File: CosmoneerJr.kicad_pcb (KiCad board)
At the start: 2 copper layers, 70 x 50 mm, 93 parts, among them J1 Header, J12 Header, J13 Header, J16 Header, J17 Header, J18 Header, J4 Header, J5 Header, J8 Header, J9 Header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

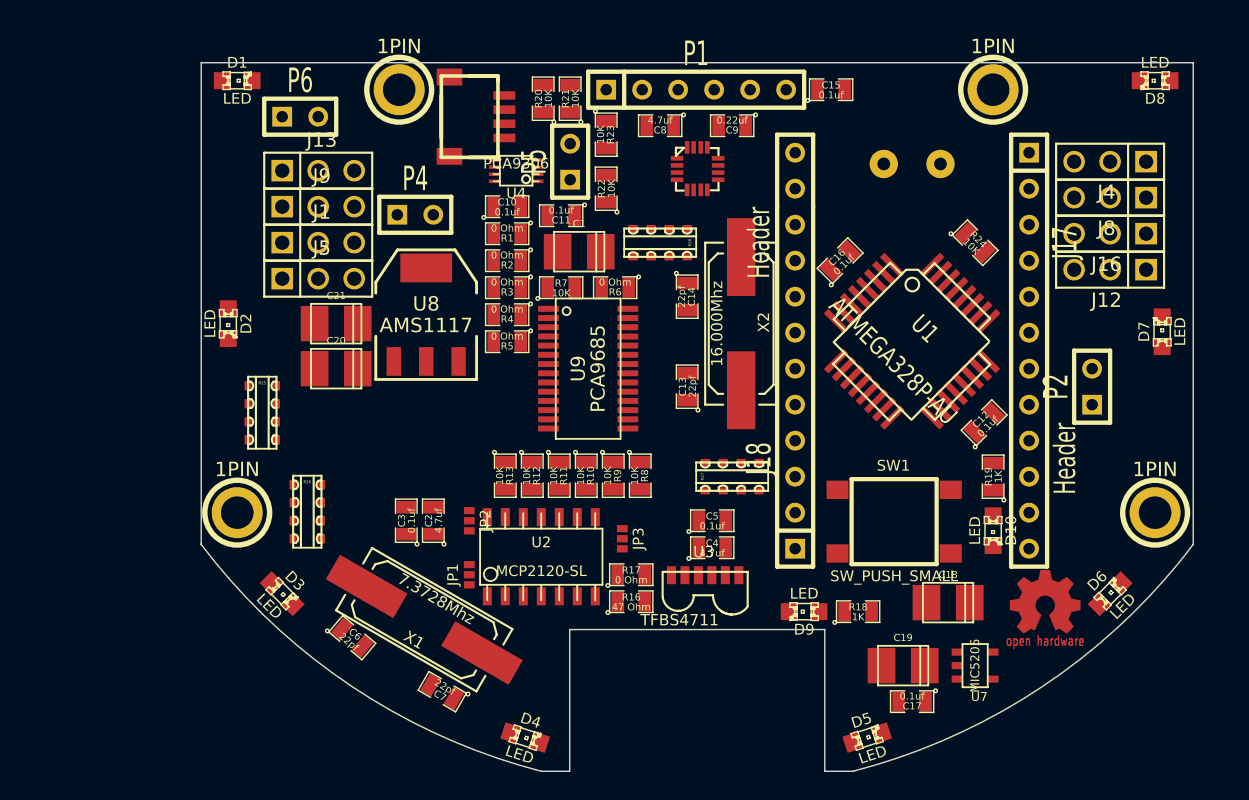
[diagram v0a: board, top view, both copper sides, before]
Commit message: PDF added
Generated a pdf version of the schematic

Schematic fixes made

Net connections on U1 were disconnected during component move.  Nets
reconnected, pdf generated, netlist generated and re-imported into pcb.
PCB file updated and saved.
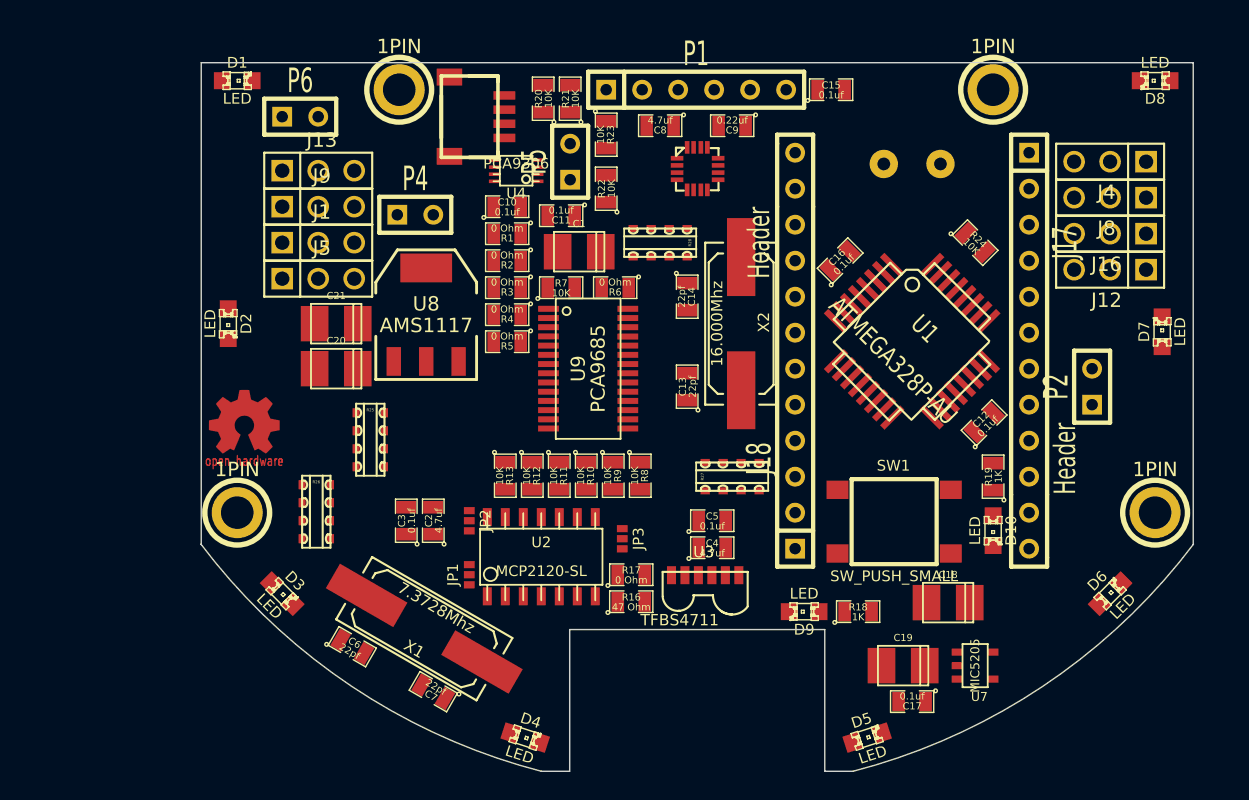
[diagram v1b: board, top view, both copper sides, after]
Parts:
- moved G*** 57.9 mm to (193.0, 140.3)
- moved R25 7.85 mm to (201.9, 141.6)
- moved C6 0.64 mm to (200.7, 156.2), turned to 330 degrees
- moved C7 0.63 mm to (206.4, 159.4)
- moved R26 0.63 mm to (198.1, 146.7)
- moved X1 0.63 mm to (205.7, 154.9)
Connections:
- J17 pad 10: (no net) -> /D7
- J17 pad 6: (no net) -> /D3
- J17 pad 9: (no net) -> /D6
- U1 pad 1: (no net) -> /D3
- U1 pad 10: (no net) -> /D6
- U1 pad 11: (no net) -> /D7
- U1 pad 2: (no net) -> /PIEZO
- U1 pad 30: (no net) -> /RXI
- U1 pad 31: (no net) -> /TXO
- U1 pad 32: (no net) -> /INT
- U1 pad 9: (no net) -> ENABLE

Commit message: Pressfit PCB additions
Added pads, drills and Silkscreen outlines for press fit pcb additions.
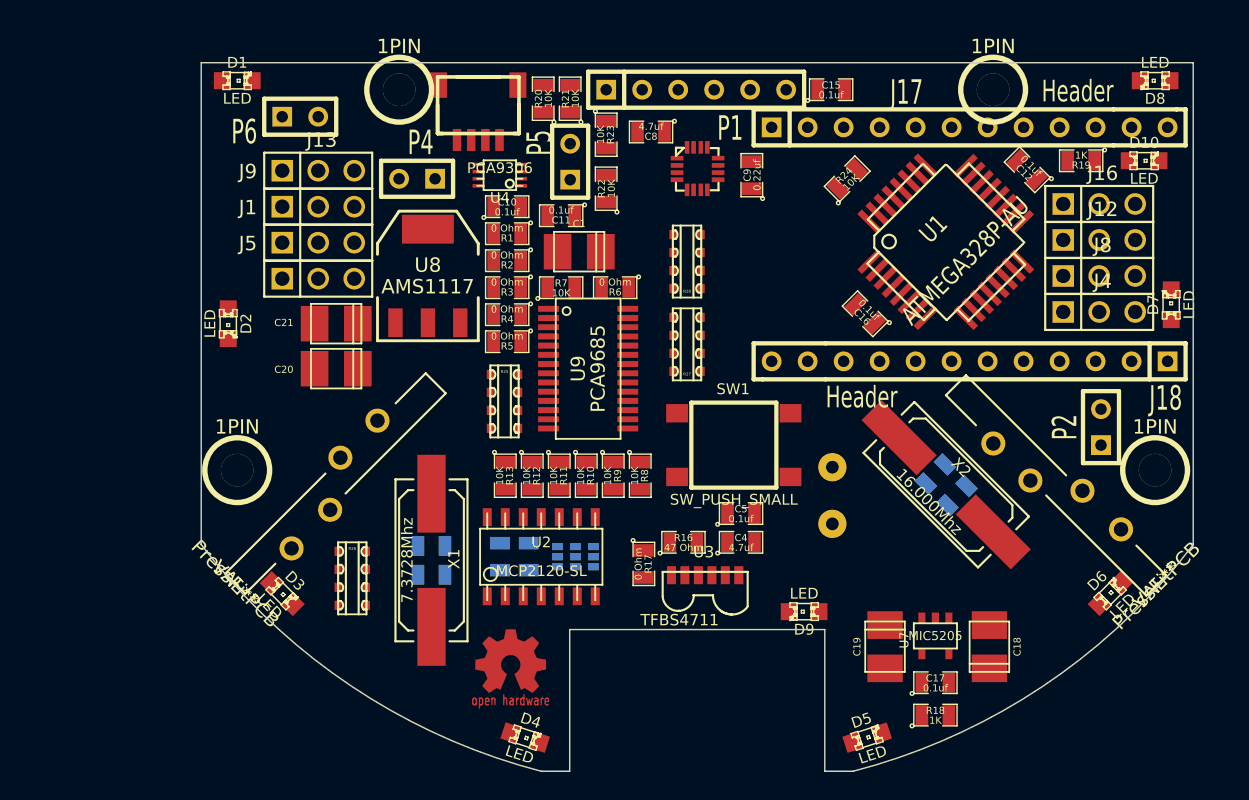
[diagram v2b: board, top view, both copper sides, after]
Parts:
- added PressFitPCB: VAL**, PressFitPCB, F.Cu at (257.4, 151.9)
- added PressFitPCB: VAL**, PressFitPCB, F.Cu at (192.4, 151.8)
- C13, C14, C2, C3, C6, C7, JP1, JP2, JP3: moved to B.Cu
- U9: footprint tssop-28 -> PCA9685
- moved D10 28.2 mm to (256.5, 121.9), turned to 0 degrees
- moved G*** 25.3 mm to (211.8, 157.2)
- moved R19 23.1 mm to (252.1, 121.9), turned to 180 degrees
- moved C14 21.5 mm to (241.8, 144.0), turned to 225 degrees
- moved PZ1 20.6 mm to (224.5, 145.5), turned to 90 degrees
- moved C13 20.5 mm to (243.3, 145.5), turned to 225 degrees
- moved X2 18.4 mm to (242.6, 144.8), turned to 315 degrees
- moved C12 18.1 mm to (248.3, 122.6), turned to 135 degrees
- moved J17 16.3 mm to (244.2, 119.6), turned to 0 degrees
- moved SW1 12.5 mm to (227.6, 142.0)
- moved J18 12.3 mm to (244.2, 136.1), turned to 180 degrees
- moved J4 10.6 mm to (253.4, 132.6), turned to 0 degrees
- moved C7 10.3 mm to (206.2, 149.1), turned to 0 degrees
- moved R24 10.1 mm to (235.6, 123.2), turned to 45 degrees
- moved R27 9.86 mm to (224.3, 134.9), turned to 180 degrees
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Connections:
- U2 pad 11: (no net) -> /A0
- U2 pad 12: (no net) -> /A1

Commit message: Moved parts and run lines
Moved several parts and began running traces.  Added two additional
internal layers, bringing the board to a total of four layers.
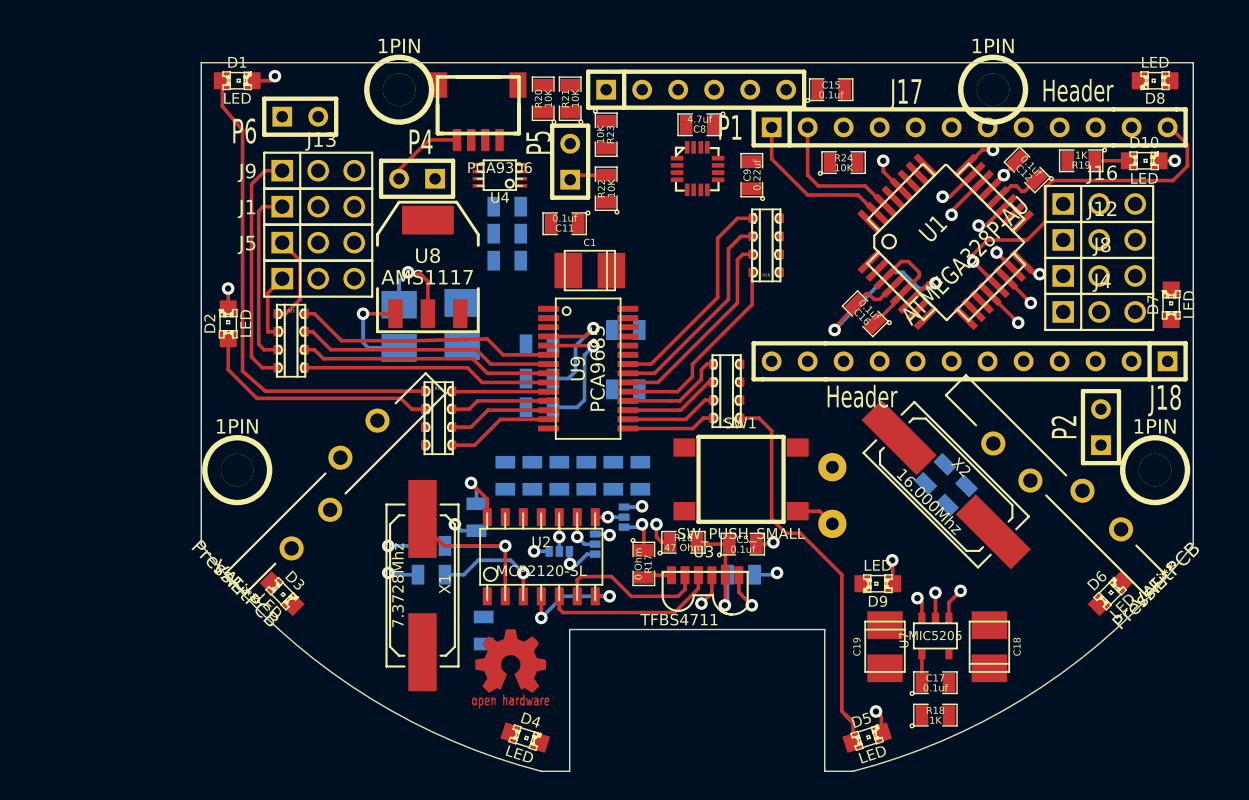
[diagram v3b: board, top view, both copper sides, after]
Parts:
- C10, C20, C21, C4, R1, R10, R11, R12, R13, R2, R3, R4, R5, R6, R7, R8, R9: moved to B.Cu
- moved R25 15.7 mm to (196.3, 134.6)
- moved R26 12.8 mm to (206.8, 140.1)
- moved C21 8.88 mm to (208.4, 133.5), turned to 90 degrees
- moved R7 8.50 mm to (220.0, 138.0)
- moved C2 6.10 mm to (209.9, 155.1), turned to 270 degrees
- moved R28 5.70 mm to (229.9, 127.9)
- moved D9 5.56 mm to (237.7, 151.8)
- moved C20 5.35 mm to (204.0, 133.6), turned to 90 degrees
- moved R5 5.16 mm to (213.9, 139.3)
- moved R4 5.05 mm to (213.9, 137.3)
- moved R3 4.60 mm to (213.9, 134.9)
- moved R27 4.33 mm to (227.1, 138.2)
- moved JP2 3.53 mm to (219.8, 147.1)
- moved C8 3.47 mm to (225.2, 119.4)
- moved C3 3.25 mm to (209.4, 147.1)
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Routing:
- net GND: track 0.00 -> 49.7 mm, vias 0 -> 17
- net N-0000040: track 0.00 -> 34.4 mm
- net N-0000044: track 0.00 -> 28.3 mm
- net +5V: track 0.00 -> 28.2 mm, vias 0 -> 6
- net /D9: track 0.00 -> 25.5 mm, vias 0 -> 1
- net /SERVO1_PWM: track 0.00 -> 18.4 mm
- net /MOTOR1_PWM: track 0.00 -> 18.1 mm
- net /SERVO2_PWM: track 0.00 -> 17.9 mm
- net /MOTOR2_PWM: track 0.00 -> 17.6 mm
- net N-0000041: track 0.00 -> 17.2 mm
- net N-0000056: track 0.00 -> 16.9 mm
- net /MOTOR4_PWM: track 0.00 -> 15.5 mm
- net /SERVO4_PWM: track 0.00 -> 14.9 mm
- net N-0000076: track 0.00 -> 14.7 mm, vias 0 -> 1
- net /MOTOR3_PWM: track 0.00 -> 14.3 mm
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- added copper zone on Inner2.Cu, net +5V
- added copper zone on Inner1.Cu, net GND
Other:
- copper layers 2 -> 4
- net class VCC added: clearance 0.254, trace_width 2.54, via_dia 0.889, via_drill 0.635

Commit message: new changes
More routing and parts movement
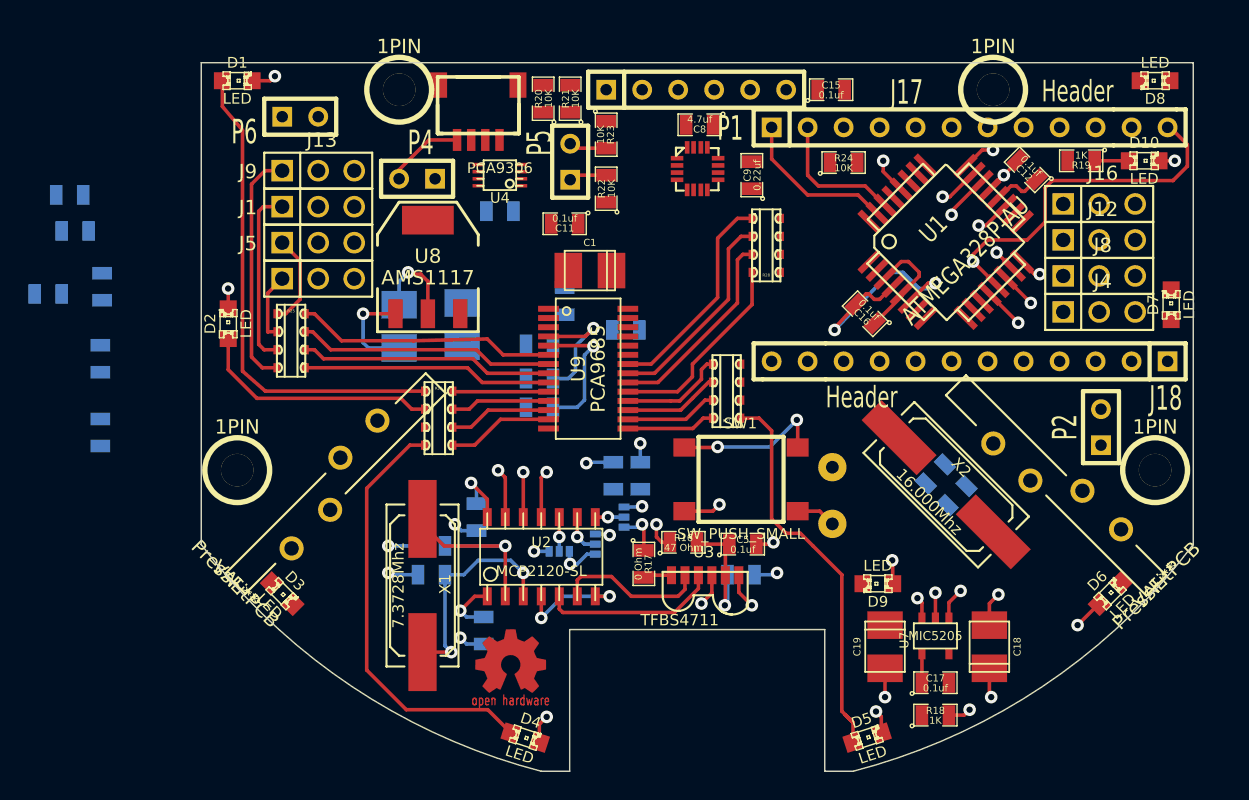
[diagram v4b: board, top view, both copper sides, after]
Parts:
- moved R7 41.3 mm to (179.2, 131.3)
- moved R11 34.9 mm to (183.0, 130.8)
- moved R12 31.6 mm to (182.9, 135.9)
- moved R1 31.0 mm to (180.7, 124.3)
- moved R2 30.6 mm to (181.1, 126.9)
- moved R13 28.7 mm to (182.9, 141.1)
- moved R10 12.4 mm to (215.6, 131.8)
- moved C10 0.61 mm to (211.1, 125.5)
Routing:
- net N-0000043: track 0.00 -> 30.2 mm
- net GND: track 49.7 -> 64.1 mm, vias 17 -> 24
- net /RESET: track 8.30 -> 19.0 mm, vias 2 -> 4
- net +5V: track 28.2 -> 36.0 mm, vias 6 -> 9
- net N-0000077: track 7.96 -> 15.6 mm, vias 1 -> 2
- net ENABLE: track 0.00 -> 3.51 mm, vias 0 -> 1
- net /A0: track 3.15 -> 6.49 mm, vias 1 -> 2
- net /A1: track 2.40 -> 5.58 mm, vias 1 -> 2
- net /I2C_SDA_3V3: track 0.00 -> 2.67 mm
- net N-0000045: track 0.00 -> 2.16 mm, vias 0 -> 1

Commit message: Final changes
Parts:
- removed 1PIN (x4): P***, Mhole
- removed G***: LOGO, Logo_copper_OSHW_6x6mm
- removed J12, J16, J4, J8: Header, PIN_ARRAY_3X1
- removed R1, R2, R3, R4, R5, R6: 0 Ohm, SM0805
- removed R10, R11, R12, R13, R8, R9: 10K, SM0805
- added JP4: JUMPER3, S_JUMPER_3, B.Cu at (217.4, 132.2)
- added JP5: JUMPER3, S_JUMPER_3, B.Cu at (217.4, 134.6)
- added P7: CONN_2, SIL-2, F.Cu at (226.2, 128.0)
- added P8: CONN_2, SIL-2, F.Cu at (226.2, 131.2)
- C11, J1, J13, J5, J9, P1: moved to B.Cu
- C4: moved to F.Cu
- moved R7 39.0 mm to (217.3, 139.6), turned to 90 degrees
- moved P2 14.3 mm to (258.2, 127.3)
- moved R20 11.7 mm to (202.4, 118.4), turned to 270 degrees
- moved R21 11.3 mm to (205.0, 119.9)
- moved R18 10.5 mm to (238.3, 151.1), turned to 90 degrees
- moved R28 9.83 mm to (224.5, 136.1)
- moved JP2 6.13 mm to (214.8, 150.5), turned to 180 degrees
- moved C11 5.96 mm to (213.0, 121.0), turned to 0 degrees
- moved R27 4.17 mm to (224.5, 141.5)
- moved SW1 3.92 mm to (231.6, 142.7), turned to 270 degrees
- moved D9 3.79 mm to (234.1, 152.7)
- moved C13 2.98 mm to (245.2, 147.8)
- moved C14 2.98 mm to (243.7, 146.3)
- moved X2 2.88 mm to (244.5, 146.9)
- moved JP3 2.71 mm to (212.6, 149.0), turned to 180 degrees
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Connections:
- U9 pad 24: /RA5 -> +5V
- U9 pad 3: /RA2 -> +5V
- U9 pad 4: /RA3 -> +5V
- U9 pad 5: /RA4 -> +5V
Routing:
- net VCC: track 3.90 -> 144.9 mm, vias 2 -> 4
- net ENABLE: track 3.51 -> 94.0 mm, vias 1 -> 4
- net /RESET: track 19.0 -> 104.5 mm, vias 4 -> 5
- net /I2C_SDA_5V: track 0.00 -> 84.1 mm, vias 0 -> 4
- net GND: track 64.1 -> 146.0 mm, vias 24 -> 30
- net /I2C_SCL_5V: track 8.18 -> 74.3 mm, vias 1 -> 4
- net /A1: track 5.58 -> 58.6 mm, vias 2 -> 1
- net N-0000040: track 0.00 -> 50.7 mm, vias 0 -> 2
- net N-0000039: track 0.00 -> 44.6 mm, vias 0 -> 2
- net /A0: track 6.49 -> 48.6 mm, vias 2 -> 1
- net +5V: track 36.0 -> 76.1 mm, vias 9 -> 11
- net +3.3V: track 6.50 -> 46.0 mm, vias 1 -> 4
- net /D10: track 2.50 -> 40.5 mm
- net N-0000038: track 2.16 -> 39.6 mm, vias 1 -> 2
- net /LED_SerClk: track 0.00 -> 31.4 mm, vias 0 -> 1
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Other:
- net class Default: clearance 0.254 -> 0.127
- net class VCC: trace_width 2.54 -> 1.27
- rule trace_clearance: 0.254 -> 0.127
- rule trace_min: 0.254 -> 0.12

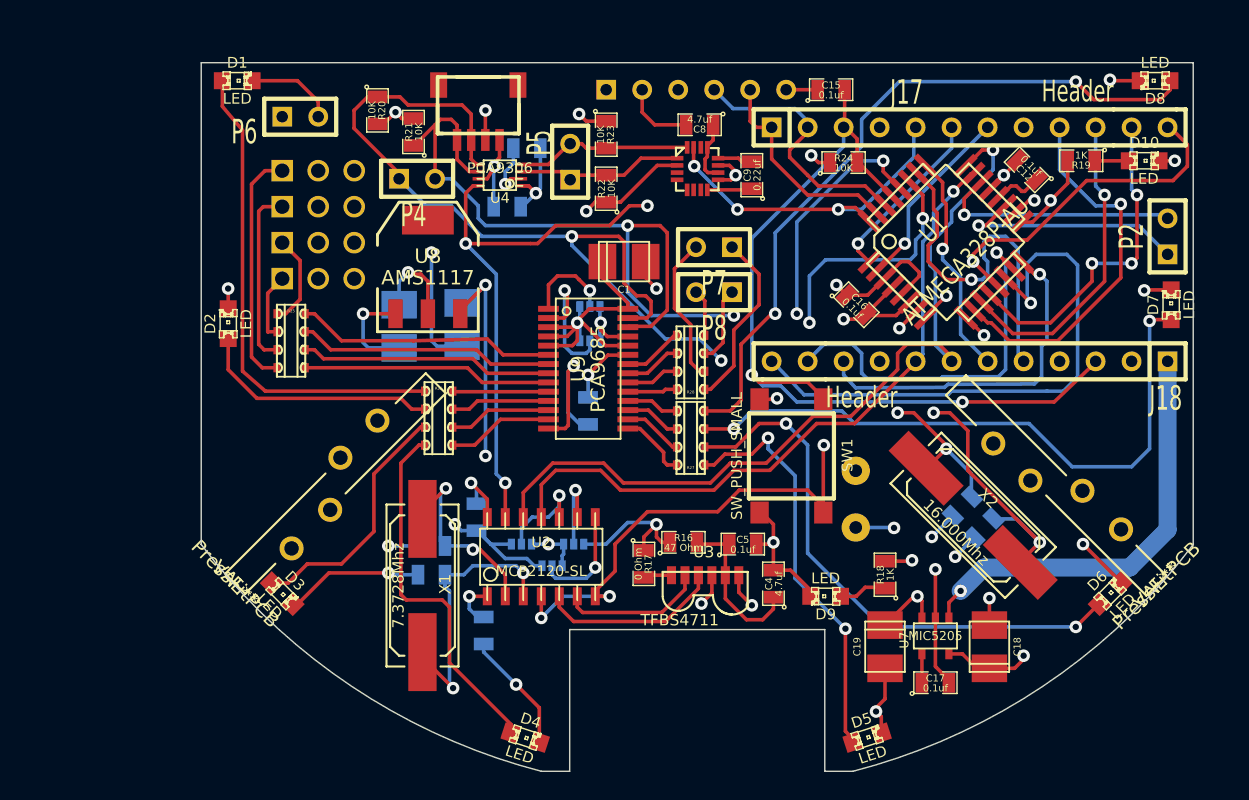
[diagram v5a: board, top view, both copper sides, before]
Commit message: Final changes
Re-added mounting holes and migrated pressFit silk screen to back side
of PCB
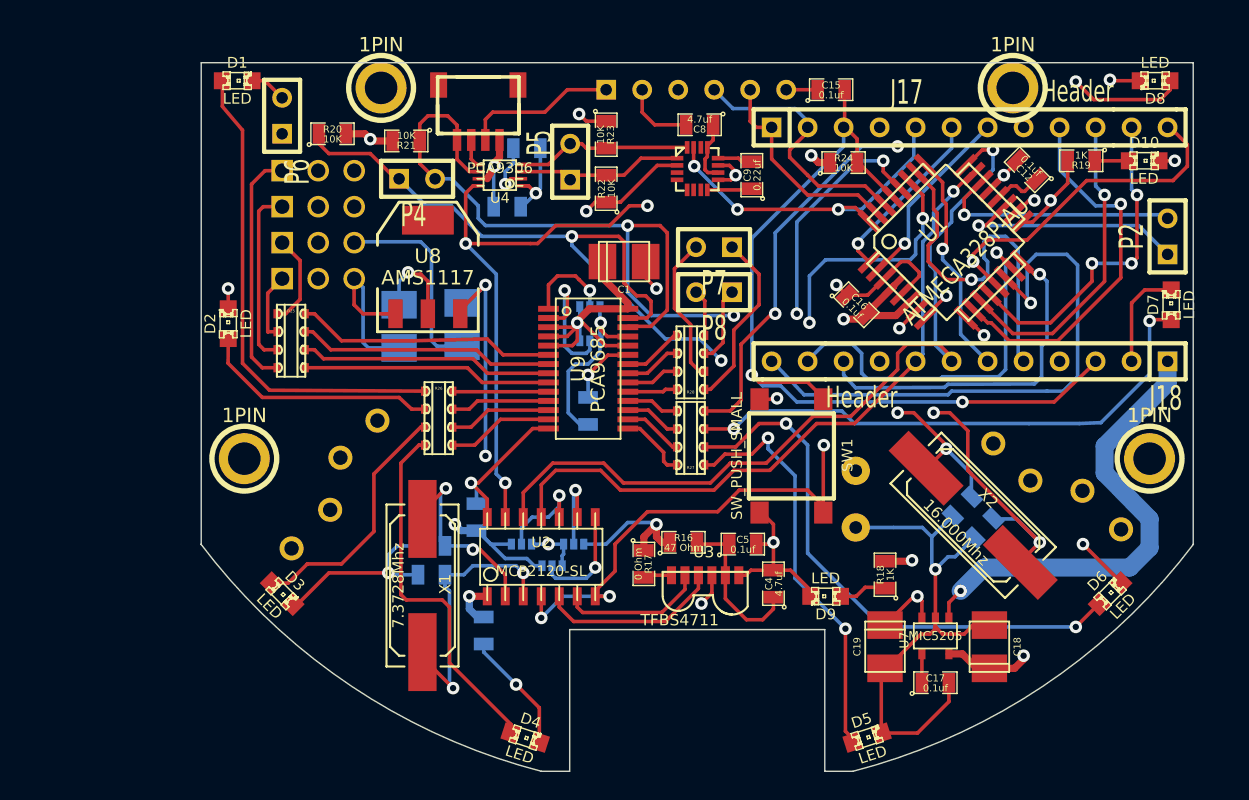
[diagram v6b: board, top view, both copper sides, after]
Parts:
- added 1PIN: P***, Mhole, F.Cu at (193.0, 142.9)
- added 1PIN: P***, Mhole, F.Cu at (256.9, 142.9)
- added 1PIN: P***, Mhole, F.Cu at (247.3, 116.8)
- added 1PIN: P***, Mhole, F.Cu at (202.7, 116.8)
- PressFitPCB (x2): moved to B.Cu
- moved R20 3.58 mm to (199.3, 120.0), turned to 0 degrees
- moved P6 1.28 mm to (195.7, 118.7), turned to 90 degrees
- moved R21 0.81 mm to (204.5, 120.5), turned to 180 degrees
- turned PressFitPCB to 135 degrees
- turned PressFitPCB to 225 degrees
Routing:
- net GND: track 146.0 -> 209.2 mm, vias 30 -> 18
- net /I2C_SDA_5V: track 84.1 -> 74.4 mm
- net N-0000039: track 44.6 -> 39.0 mm
- net VCC: track 144.9 -> 146.2 mm
- net N-0000040: track 50.7 -> 51.9 mm, vias 2 -> 3
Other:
- net class 5V added: clearance 0.127, trace_width 0.508, via_dia 0.889, via_drill 0.635
